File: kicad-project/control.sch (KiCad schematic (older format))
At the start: 5 parts, among them SW1 RST_SW, U1 RP2040

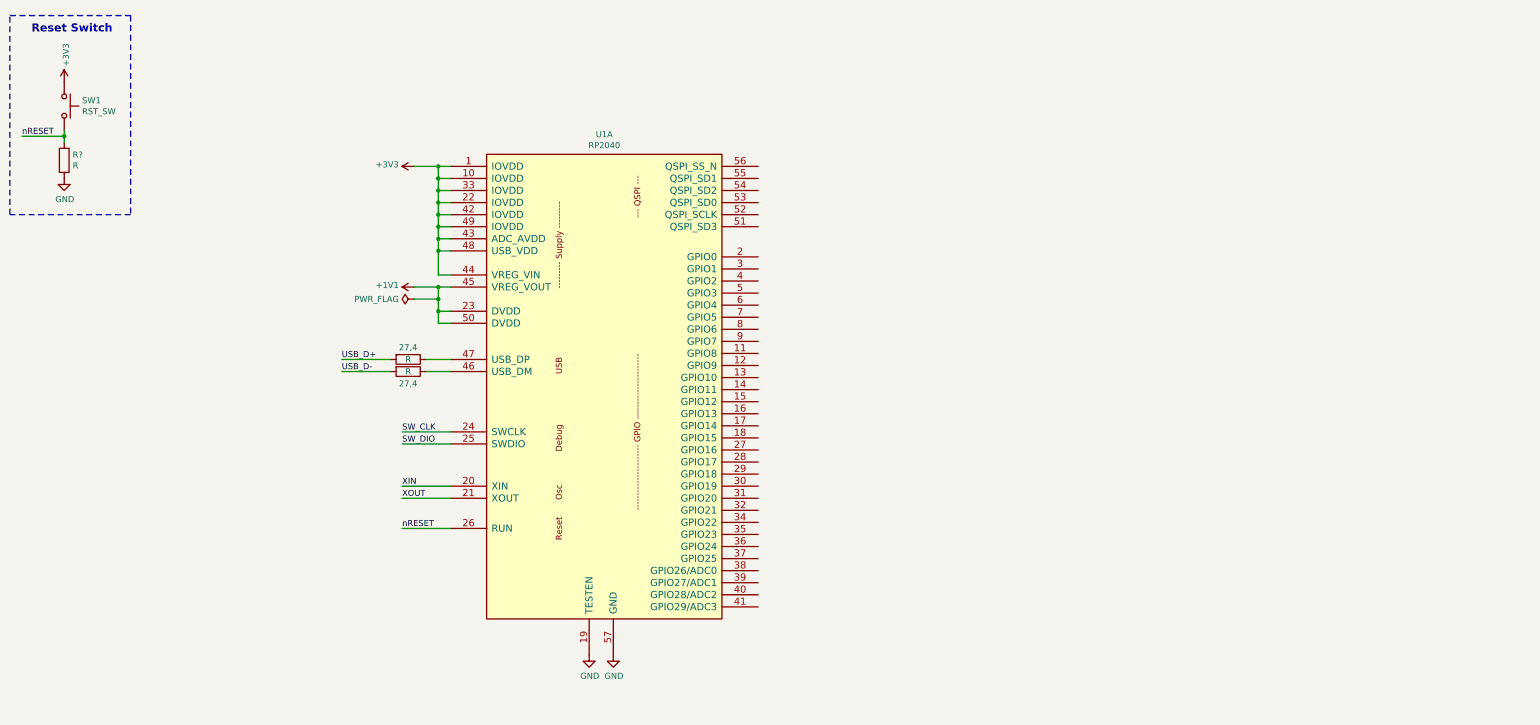
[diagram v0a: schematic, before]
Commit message: sch: add notes and circuits from 2022/03/10 lecture
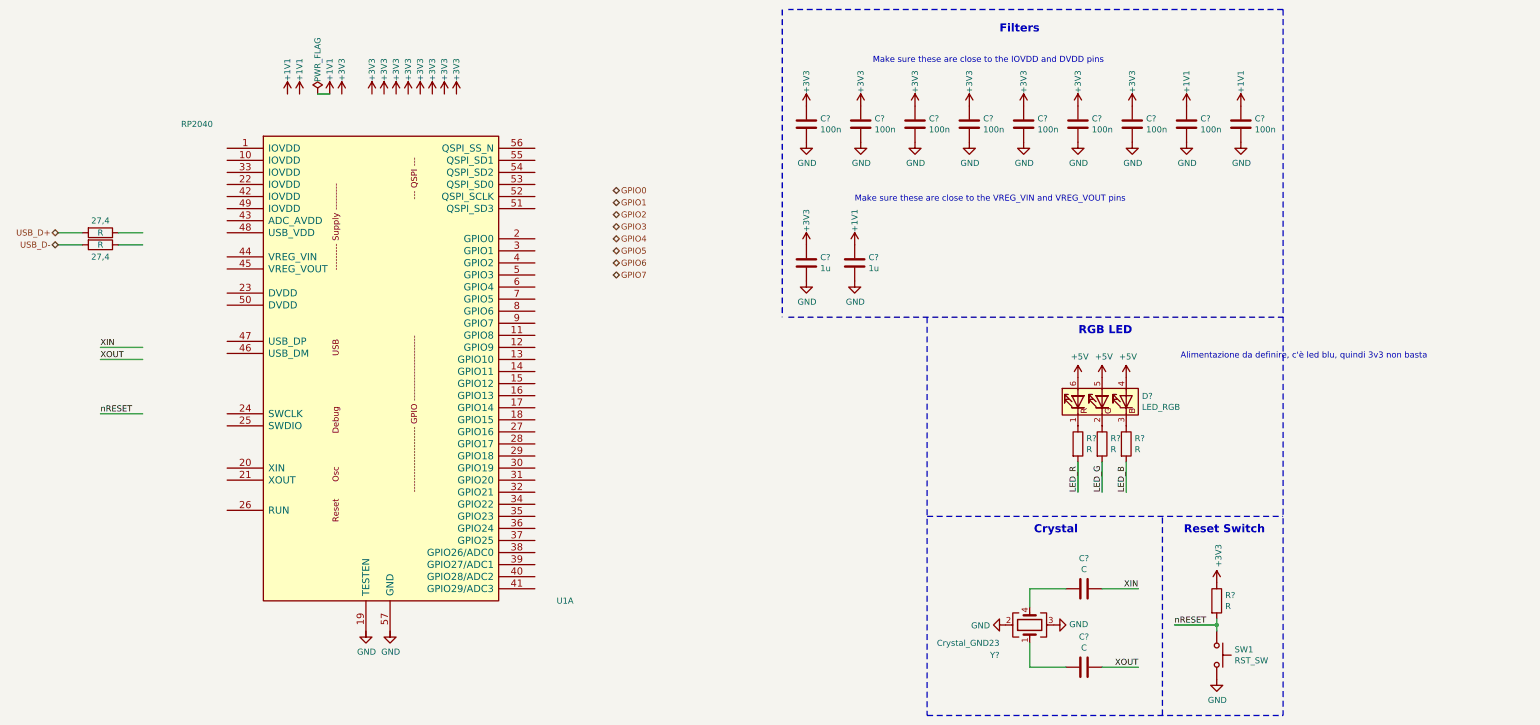
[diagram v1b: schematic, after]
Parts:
- added C? (x2): C, symbol Device:C
- added C? (x9): 100n, Capacitor_SMD:C_0603_1608Metric, symbol Device:C
- added C? (x2): 1u, Capacitor_SMD:C_0603_1608Metric, symbol Device:C
- added D?: LED_RGB, symbol Device:LED_RGB
- added R? (x3): R, symbol Device:R
- added Y?: Crystal_GND23, symbol Device:Crystal_GND23
- 27,4: footprint (none) -> Resistor_SMD:R_0603_1608Metric
- U1: footprint (none) -> AA_PSE_2021:RP2040
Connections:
- net labels added: +5V, GPIO0, GPIO1, GPIO2, GPIO3, GPIO4, GPIO5, GPIO6, GPIO7, LED_B, LED_G, LED_R
- net labels removed: SW_CLK, SW_DIO
- wire segments 38 -> 20
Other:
- note added: "Alimentazione da definire, c'è led blu, quindi 3v3 non basta"
- note added: "Crystal"
- note added: "Filters"
- note added: "Make sure these are close to the IOVDD and DVDD pins"
- note added: "Make sure these are close to the VREG_VIN and VREG_VOUT pins"
- note added: "RGB LED"
- moved on the sheet: 27,4, R?, SW1, U1A

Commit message: sch: add gps
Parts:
- removed C? (x9): 100n, Capacitor_SMD:C_0603_1608Metric, symbol Device:C
- removed C? (x2): 1u, Capacitor_SMD:C_0603_1608Metric, symbol Device:C
- U1: symbol PPSE_2021:RP2040 -> AA_PPSE_2021:RP2040
- Y?: footprint (none) -> Crystal:Crystal_SMD_3225-4Pin_3.2x2.5mm
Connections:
- net labels added: FLASH_CLK, FLASH_D0, FLASH_D1, FLASH_D2, FLASH_D3, FLASH_S_N
- wire segments 20 -> 26
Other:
- note added: "Is symbol correct?\nIs circuit correct? Don't think so"
- note removed: "Filters"
- note removed: "Make sure these are close to the IOVDD and DVDD pins"
- note removed: "Make sure these are close to the VREG_VIN and VREG_VOUT pins"
